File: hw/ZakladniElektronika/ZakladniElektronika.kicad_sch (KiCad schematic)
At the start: 0 parts

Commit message: Nastin schematu
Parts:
- added J5, J6: Conn_01x08, Connector_JST:JST_EH_B8B-EH-A_1x08_P2.50mm_Vertical, symbol Connector_Generic:Conn_01x08
- added J7, J8: Conn_01x32, Connector_FFC-FPC:TE_3-1734839-2_1x32-1MP_P0.5mm_Horizontal, symbol Connector_Generic:Conn_01x32
- added J9: Conn_01x01, Connector_PinHeader_2.54mm:PinHeader_1x01_P2.54mm_Vertical, symbol Connector_Generic:Conn_01x01
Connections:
- net LedDeska/3V3: now also J7.28 (Pin_28)
- net LedDeska/5V: now also J7.1 (Pin_1), J7.10 (Pin_10), J7.11 (Pin_11), J7.12 (Pin_12), J7.13 (Pin_13), J7.2 (Pin_2), J7.3 (Pin_3), J7.4 (Pin_4), J7.5 (Pin_5), J7.6 (Pin_6), J7.7 (Pin_7), J7.8 (Pin_8), J7.9 (Pin_9)
- net LedDeska/AN-GND: now also J7.32 (Pin_32)
- net LedDeska/INT-LDC: now also J7.29 (Pin_29)
- net LedDeska/LED-GND: now also J7.15 (Pin_15), J7.16 (Pin_16), J7.17 (Pin_17), J7.18 (Pin_18), J7.19 (Pin_19), J7.20 (Pin_20), J7.21 (Pin_21), J7.22 (Pin_22), J7.23 (Pin_23), J7.24 (Pin_24), J7.25 (Pin_25), J7.26 (Pin_26), J7.27 (Pin_27)
- net LedDeska/SCL: now also J7.31 (Pin_31)
- net LedDeska/SDA: now also J7.30 (Pin_30)
- net LedDeska/WS2812: now also J7.14 (Pin_14)
- new net HlavniDeska/3V3: J8.28 (Pin_28)
- new net HlavniDeska/5V: J8.1 (Pin_1), J8.10 (Pin_10), J8.11 (Pin_11), J8.12 (Pin_12), J8.13 (Pin_13), J8.2 (Pin_2), J8.3 (Pin_3), J8.4 (Pin_4), J8.5 (Pin_5), J8.6 (Pin_6), J8.7 (Pin_7), J8.8 (Pin_8), J8.9 (Pin_9)
- new net HlavniDeska/ESP_BOOT: J5.2 (Pin_2)
- new net HlavniDeska/GND: J5.8 (Pin_8), J8.15 (Pin_15), J8.16 (Pin_16), J8.17 (Pin_17), J8.18 (Pin_18), J8.19 (Pin_19), J8.20 (Pin_20), J8.21 (Pin_21), J8.22 (Pin_22), J8.23 (Pin_23), J8.24 (Pin_24), J8.25 (Pin_25), J8.26 (Pin_26), J8.27 (Pin_27), J8.32 (Pin_32)
- new net HlavniDeska/INT: J8.29 (Pin_29)
- new net HlavniDeska/IO35: J5.4 (Pin_4)
- new net HlavniDeska/IO36: J5.5 (Pin_5)
- new net HlavniDeska/IO37: J5.6 (Pin_6)
- new net HlavniDeska/IO38: J5.7 (Pin_7)
- new net HlavniDeska/IO39: J8.14 (Pin_14)
- new net HlavniDeska/IO40: J9.1 (Pin_1)
- new net HlavniDeska/ON: J5.1 (Pin_1)
- new net HlavniDeska/RST: J5.3 (Pin_3)
- new net HlavniDeska/SCL: J8.31 (Pin_31)
- new net HlavniDeska/SDA: J8.30 (Pin_30)
- new net MiniUI/BOOT: J6.2 (Pin_2)
- new net MiniUI/GND: J6.8 (Pin_8)
- new net MiniUI/LED1: J6.7 (Pin_7)
- new net MiniUI/LED2: J6.6 (Pin_6)
- new net MiniUI/ON: J6.1 (Pin_1)
- new net MiniUI/RST: J6.3 (Pin_3)
- new net MiniUI/SW1: J6.4 (Pin_4)
- new net MiniUI/SW2: J6.5 (Pin_5)
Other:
- sheet HlavniDeska ports: added 3V3, 5V, ESP_BOOT, GND, INT, IO35, IO36, IO37, IO38, IO39, IO40, ON, RST, SCL, SDA; removed none
- sheet MiniUI: file MiniUI/MiniUI.kicad_sch -> MiniUI.kicad_sch
- sheet MiniUI ports: added BOOT, GND, LED1, LED2, ON, RST, SW1, SW2; removed none

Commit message: Zaciame psat
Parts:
- removed J9: Conn_01x01, Connector_PinHeader_2.54mm:PinHeader_1x01_P2.54mm_Vertical, symbol Connector_Generic:Conn_01x01
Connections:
- net HlavniDeska/IO35 is gone; now on net HlavniDeska/IO36: J5.4 (Pin_4)
- net HlavniDeska/5V: no longer J8.13 (Pin_13)
- net HlavniDeska/GND: now also J8.13 (Pin_13), J8.14 (Pin_14), J8.29 (Pin_29); no longer J8.25 (Pin_25), J8.26 (Pin_26), J8.27 (Pin_27), J8.32 (Pin_32)
- net HlavniDeska/INT: now also J8.30 (Pin_30); no longer J8.29 (Pin_29)
- net HlavniDeska/IO36: no longer J5.5 (Pin_5)
- net HlavniDeska/IO37: now also J5.5 (Pin_5); no longer J5.6 (Pin_6)
- net HlavniDeska/IO38: now also J5.6 (Pin_6); no longer J5.7 (Pin_7)
- net HlavniDeska/IO39: now also J8.25 (Pin_25); no longer J8.14 (Pin_14)
- net HlavniDeska/IO40: now also J5.7 (Pin_7)
- net HlavniDeska/SCL: now also J8.32 (Pin_32); no longer J8.31 (Pin_31)
- net HlavniDeska/SDA: now also J8.31 (Pin_31); no longer J8.30 (Pin_30)
- net LedDeska/5V: no longer J7.13 (Pin_13)
- net LedDeska/AN-GND: now also J7.29 (Pin_29); no longer J7.32 (Pin_32)
- net LedDeska/INT-LDC: now also J7.30 (Pin_30); no longer J7.29 (Pin_29)
- net LedDeska/LED-GND: now also J7.13 (Pin_13), J7.14 (Pin_14); no longer J7.25 (Pin_25), J7.26 (Pin_26), J7.27 (Pin_27)
- net LedDeska/SCL: now also J7.32 (Pin_32); no longer J7.31 (Pin_31)
- net LedDeska/SDA: now also J7.31 (Pin_31); no longer J7.30 (Pin_30)
- net LedDeska/WS2812: now also J7.25 (Pin_25); no longer J7.14 (Pin_14)
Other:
- sheet HlavniDeska ports: added none; removed IO35

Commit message: WIP
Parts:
- removed J7, J8: Conn_01x32, Connector_FFC-FPC:TE_3-1734839-2_1x32-1MP_P0.5mm_Horizontal, symbol Connector_Generic:Conn_01x32
- added J10: Conn_01x40, Connector_FFC-FPC:Molex_52559-3652_2x18-1MP_P0.5mm_Vertical, symbol Connector_Generic:Conn_01x40
- added J11: Conn_01x40, Connector_FFC-FPC:Hirose_FH12-40S-0.5SH_1x40-1MP_P0.50mm_Horizontal, symbol Connector_Generic:Conn_01x40
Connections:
- net HlavniDeska/3V3: now also J11.36 (Pin_36)
- net HlavniDeska/5V: now also J11.1 (Pin_1), J11.10 (Pin_10), J11.11 (Pin_11), J11.12 (Pin_12), J11.13 (Pin_13), J11.2 (Pin_2), J11.3 (Pin_3), J11.4 (Pin_4), J11.5 (Pin_5), J11.6 (Pin_6), J11.7 (Pin_7), J11.8 (Pin_8), J11.9 (Pin_9)
- net HlavniDeska/GND: now also J11.14 (Pin_14), J11.15 (Pin_15), J11.16 (Pin_16), J11.17 (Pin_17), J11.18 (Pin_18), J11.19 (Pin_19), J11.20 (Pin_20), J11.21 (Pin_21), J11.22 (Pin_22), J11.23 (Pin_23), J11.24 (Pin_24), J11.25 (Pin_25), J11.26 (Pin_26), J11.37 (Pin_37)
- net HlavniDeska/INT: now also J11.38 (Pin_38)
- net HlavniDeska/IO39: now also J11.27 (Pin_27)
- net HlavniDeska/SCL: now also J11.40 (Pin_40)
- net HlavniDeska/SDA: now also J11.39 (Pin_39)
- net LedDeska/3V3: now also J10.36 (Pin_36)
- net LedDeska/5V: now also J10.1 (Pin_1), J10.10 (Pin_10), J10.11 (Pin_11), J10.12 (Pin_12), J10.13 (Pin_13), J10.2 (Pin_2), J10.3 (Pin_3), J10.4 (Pin_4), J10.5 (Pin_5), J10.6 (Pin_6), J10.7 (Pin_7), J10.8 (Pin_8), J10.9 (Pin_9)
- net LedDeska/AN-GND: now also J10.37 (Pin_37)
- net LedDeska/INT-LDC: now also J10.38 (Pin_38)
- net LedDeska/LED-GND: now also J10.14 (Pin_14), J10.15 (Pin_15), J10.16 (Pin_16), J10.17 (Pin_17), J10.18 (Pin_18), J10.19 (Pin_19), J10.20 (Pin_20), J10.21 (Pin_21), J10.22 (Pin_22), J10.23 (Pin_23), J10.24 (Pin_24), J10.25 (Pin_25), J10.26 (Pin_26)
- net LedDeska/SCL: now also J10.40 (Pin_40)
- net LedDeska/SDA: now also J10.39 (Pin_39)
- net LedDeska/WS2812: now also J10.27 (Pin_27)
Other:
- note added: "rezervováno"
- moved on the sheet: J5, J6

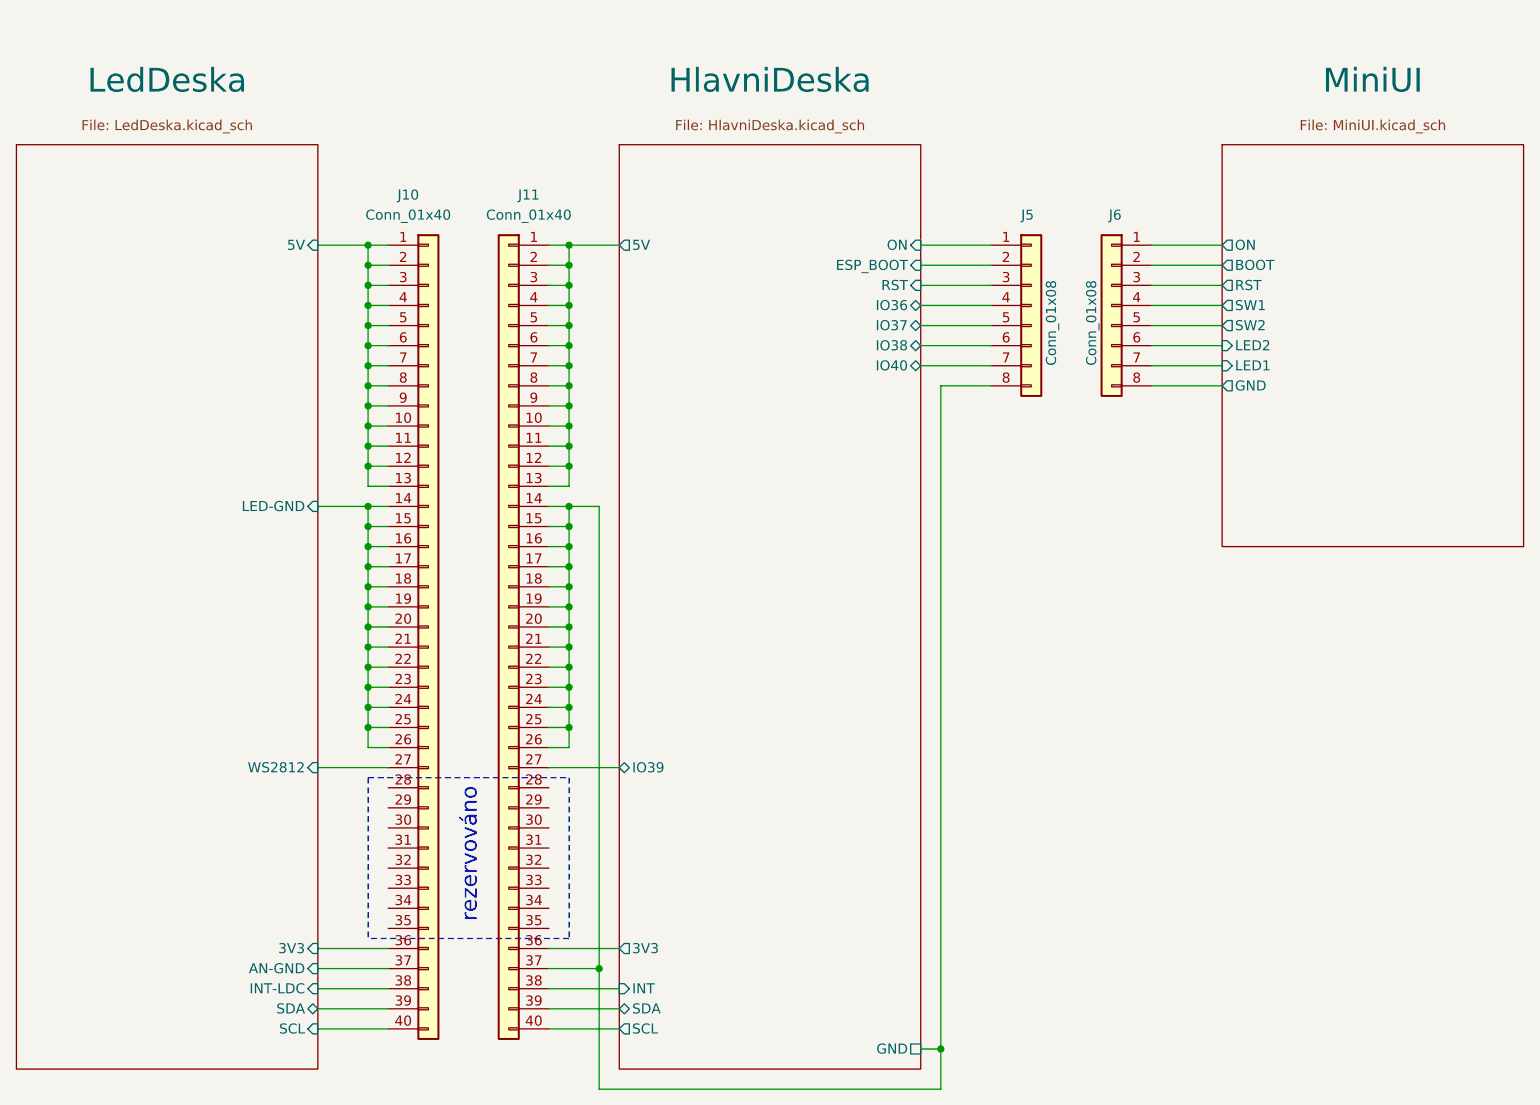
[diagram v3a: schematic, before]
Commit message: Likvidace MiniUI jako samostatné desky a výběr všech komponent
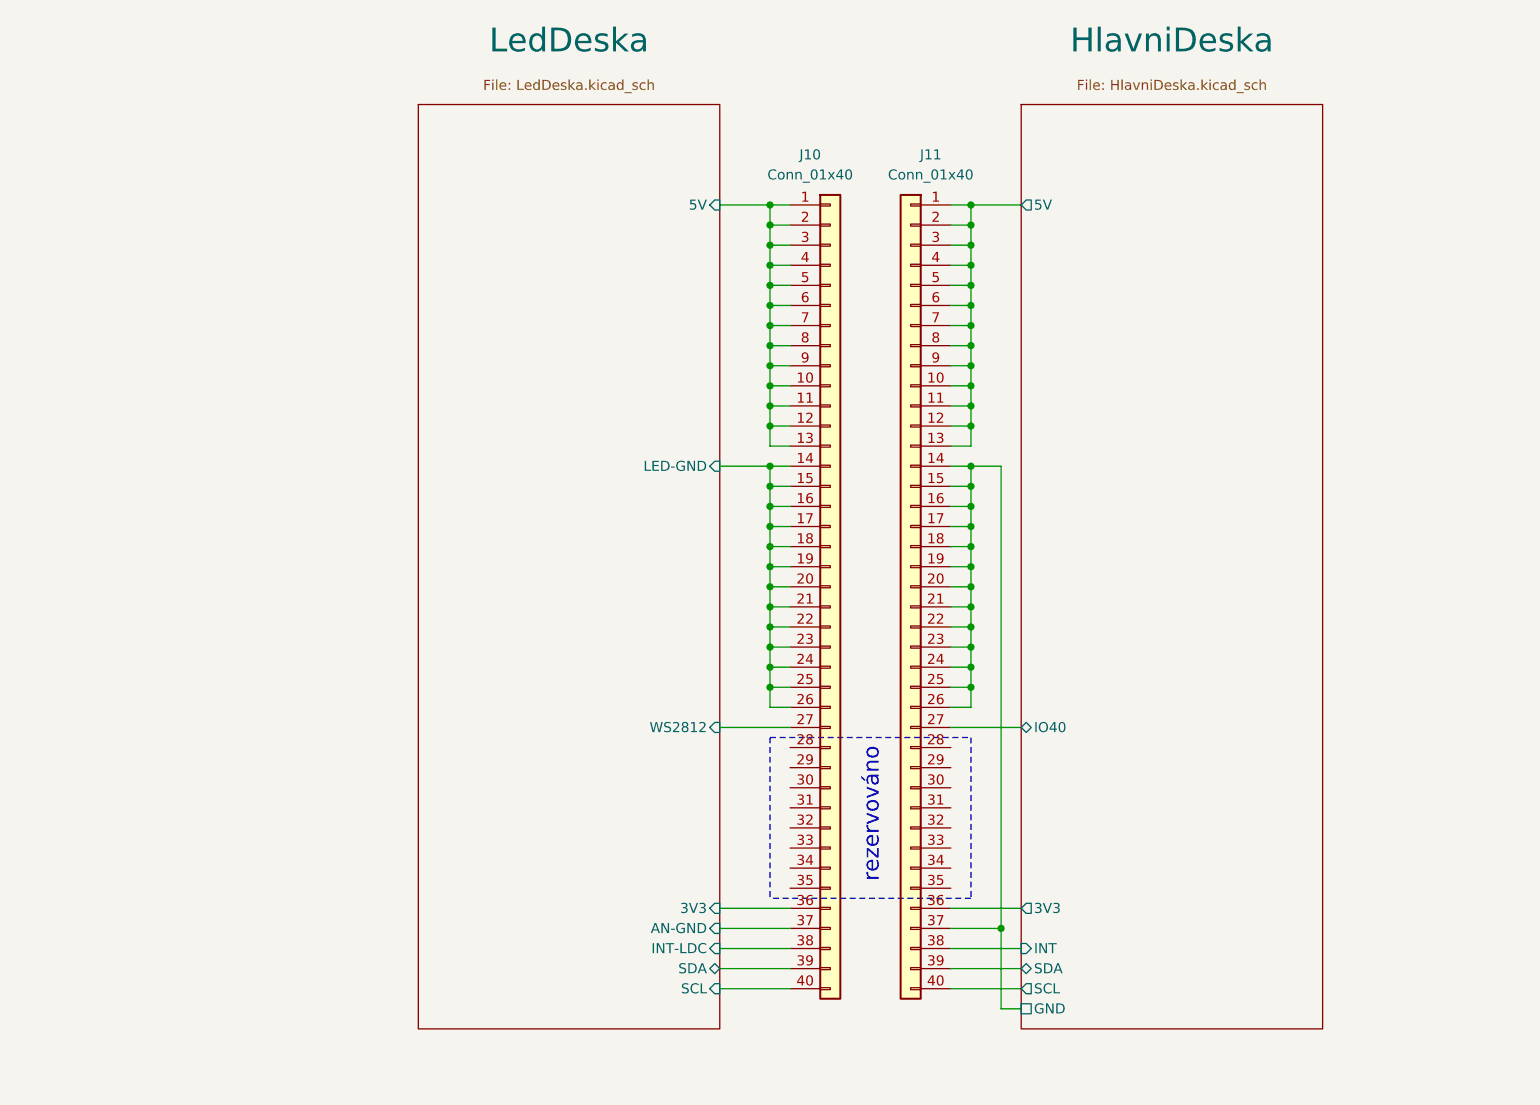
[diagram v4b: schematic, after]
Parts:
- removed J5, J6: Conn_01x08, Connector_JST:JST_EH_B8B-EH-A_1x08_P2.50mm_Vertical, symbol Connector_Generic:Conn_01x08
- J10, J11: Basic/Extended (none) -> E
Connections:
- net HlavniDeska/IO39 is gone; now on net HlavniDeska/IO40: J11.27 (Pin_27)
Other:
- removed sheet MiniUI
- sheet HlavniDeska ports: added none; removed ESP_BOOT, IO36, IO37, IO38, IO39, ON, RST
- moved on the sheet: J10, J11
